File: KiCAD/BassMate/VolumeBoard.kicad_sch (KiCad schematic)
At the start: 15 parts

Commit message: Started docs
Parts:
- added #J?: AudioJack3_Dual_Switch, symbol Connector:AudioJack3_Dual_Switch
- added J?: 1x5, Connector_PinHeader_2.54mm:PinHeader_1x05_P2.54mm_Vertical, symbol Connector_Generic:Conn_01x05
- J?: value To Headphone Socket -> 1x5
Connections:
- new net: #J?.R1, J?.4 (Pin_4)
- new net: #J?.RN1, J?.5 (Pin_5)
- new net: #J?.S1, J?.1 (Pin_1)
- new net: #J?.SN1, J?.2 (Pin_2)
- new net: #J?.T1, #J?.TN1, J?.3 (Pin_3)
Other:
- note added: "Headphone socket on daughter board"
- note added: "Power and I/O"
- note added: "Volume control"
- moved on the sheet: C?, J?, R?, U?A, U?B, U?C, U?D, U?E

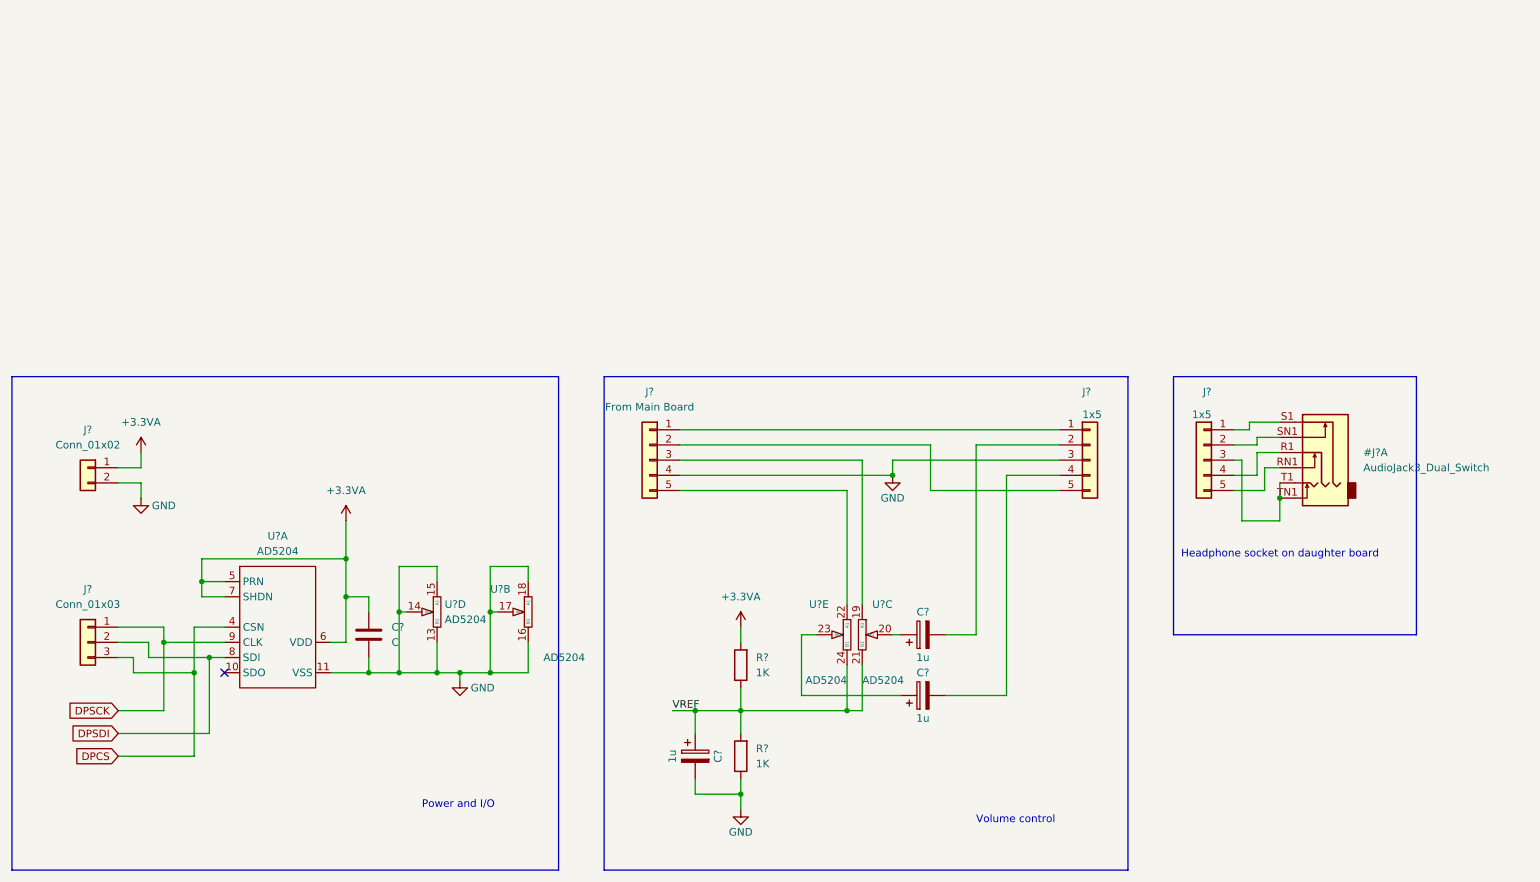
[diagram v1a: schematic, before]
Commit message: Converted most libs to git sbmodules
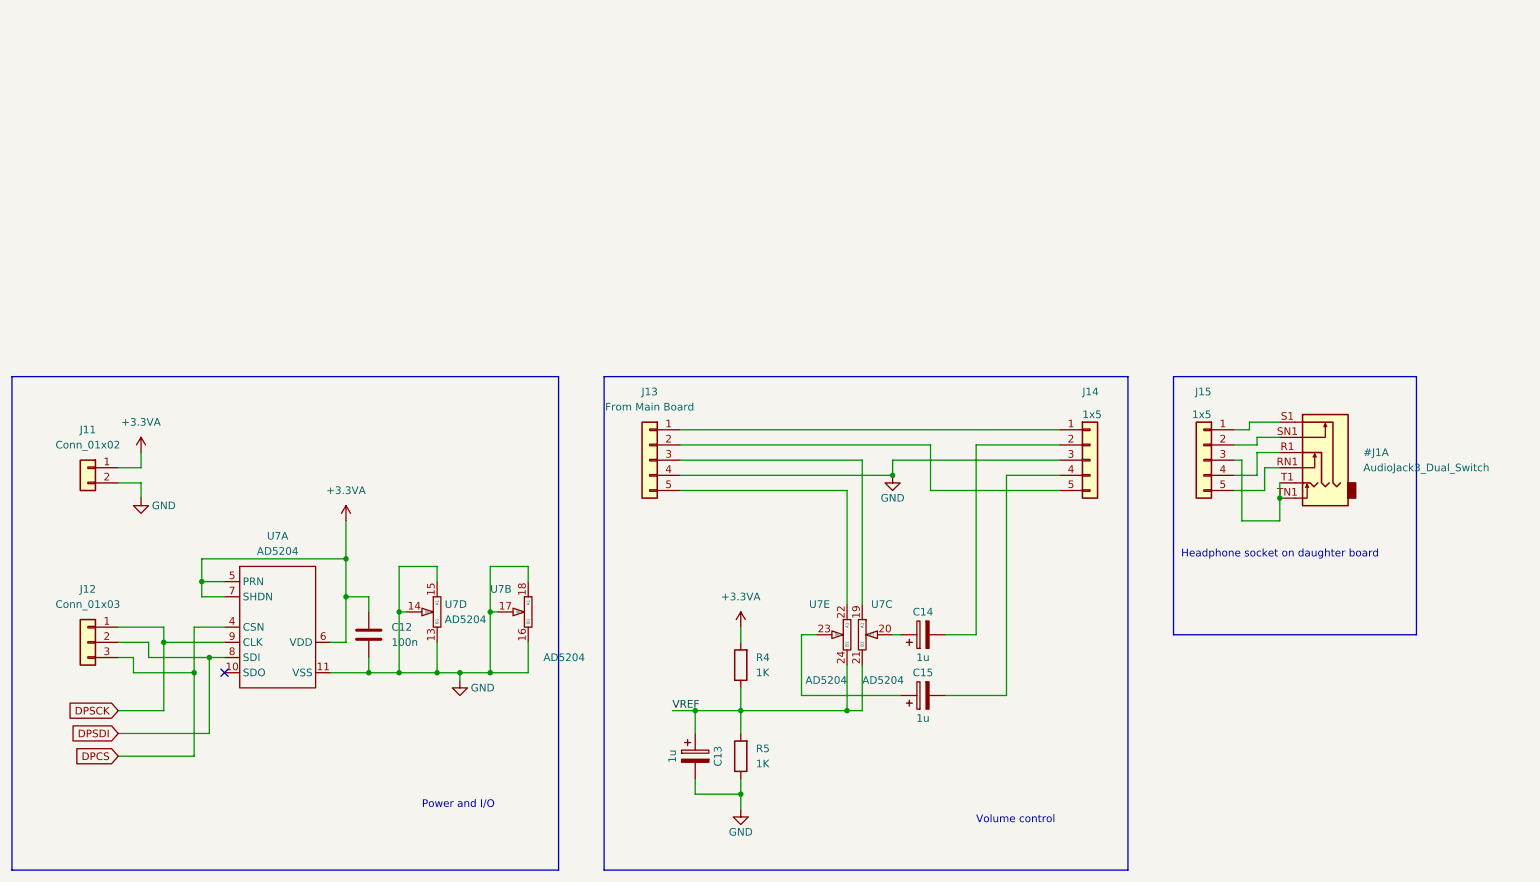
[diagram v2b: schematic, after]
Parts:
- C12: renamed from C?; value C -> 100n
- gave numbers to parts that had none: 12
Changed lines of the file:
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@@
   (symbol (lib_id "Device:C_Polarized") (at 173.99 119.38 90) (unit 1)
     (in_bom yes) (on_board yes)
-    (property "Reference" "C?" (id 0) (at 173.99 115.57 90))
+    (property "Reference" "C14" (id 0) (at 173.99 115.57 90))
     (property "Value" "1u" (id 1) (at 173.99 123.19 90))
     (property "Footprint" "Capacitor_THT:CP_Radial_D10.0mm_P3.50mm" (id 2) (at 177.8 118.4148 0)
@@
   (symbol (lib_id "power:+3.3VA") (at 43.18 88.9 0) (unit 1)
     (in_bom yes) (on_board yes) (fields_autoplaced)
-    (property "Reference" "#PWR?" (id 0) (at 43.18 92.71 0)
+    (property "Reference" "#PWR024" (id 0) (at 43.18 92.71 0)
       (effects (font (size 1.27 1.27)) hide)
     )
@@
   (symbol (lib_id "power:+3.3VA") (at 77.47 100.33 0) (unit 1)
     (in_bom yes) (on_board yes) (fields_autoplaced)
-    (property "Reference" "#PWR?" (id 0) (at 77.47 104.14 0)
+    (property "Reference" "#PWR026" (id 0) (at 77.47 104.14 0)
       (effects (font (size 1.27 1.27)) hide)
     )
@@
   (symbol (lib_id "UKMaker:AD5204") (at 107.95 115.57 0) (unit 2)
     (in_bom yes) (on_board yes)
-    (property "Reference" "U?" (id 0) (at 101.6 111.76 0)
+    (property "Reference" "U7" (id 0) (at 101.6 111.76 0)
       (effects (font (size 1.27 1.27)) (justify left))
     )
@@
   (symbol (lib_id "UKMaker:AD5204") (at 163.83 119.38 0) (mirror y) (unit 3)
     (in_bom yes) (on_board yes)
-    (property "Reference" "U?" (id 0) (at 168.91 114.3 0)
+    (property "Reference" "U7" (id 0) (at 168.91 114.3 0)
       (effects (font (size 1.27 1.27)) (justify left))
     )
@@
   (symbol (lib_id "power:+3.3VA") (at 143.51 118.11 0) (unit 1)
     (in_bom yes) (on_board yes) (fields_autoplaced)
-    (property "Reference" "#PWR?" (id 0) (at 143.51 121.92 0)
+    (property "Reference" "#PWR028" (id 0) (at 143.51 121.92 0)
       (effects (font (size 1.27 1.27)) hide)
     )
@@
   (symbol (lib_id "Connector:AudioJack3_Dual_Switch") (at 238.76 88.9 0) (mirror y) (unit 1)
     (in_bom yes) (on_board yes) (fields_autoplaced)
-    (property "Reference" "#J?" (id 0) (at 247.65 88.8999 0)
+    (property "Reference" "#J1" (id 0) (at 247.65 88.8999 0)
       (effects (font (size 1.27 1.27)) (justify right))
     )
@@
   (symbol (lib_id "Device:C") (at 81.28 119.38 0) (unit 1)
     (in_bom yes) (on_board yes) (fields_autoplaced)
-    (property "Reference" "C?" (id 0) (at 85.09 118.1099 0)
-      (effects (font (size 1.27 1.27)) (justify left))
-    )
-    (property "Value" "C" (id 1) (at 85.09 120.6499 0)
+    (property "Reference" "C12" (id 0) (at 85.09 118.1099 0)
+      (effects (font (size 1.27 1.27)) (justify left))
+    )
+    (property "Value" "100n" (id 1) (at 85.09 120.6499 0)
       (effects (font (size 1.27 1.27)) (justify left))
     )
@@
   (symbol (lib_id "Device:R") (at 143.51 139.7 180) (unit 1)
     (in_bom yes) (on_board yes) (fields_autoplaced)
-    (property "Reference" "R?" (id 0) (at 146.05 138.4299 0)
+    (property "Reference" "R5" (id 0) (at 146.05 138.4299 0)
       (effects (font (size 1.27 1.27)) (justify right))
     )
@@
   (symbol (lib_id "Device:R") (at 143.51 124.46 180) (unit 1)
     (in_bom yes) (on_board yes) (fields_autoplaced)
-    (property "Reference" "R?" (id 0) (at 146.05 123.1899 0)
+    (property "Reference" "R4" (id 0) (at 146.05 123.1899 0)
       (effects (font (size 1.27 1.27)) (justify right))
     )
@@
   (symbol (lib_id "power:GND") (at 96.52 127 0) (unit 1)
     (in_bom yes) (on_board yes)
-    (property "Reference" "#PWR?" (id 0) (at 96.52 133.35 0)
+    (property "Reference" "#PWR027" (id 0) (at 96.52 133.35 0)
       (effects (font (size 1.27 1.27)) hide)
     )
@@
   (symbol (lib_id "power:GND") (at 43.18 96.52 0) (unit 1)
     (in_bom yes) (on_board yes)
-    (property "Reference" "#PWR?" (id 0) (at 43.18 102.87 0)
+    (property "Reference" "#PWR025" (id 0) (at 43.18 102.87 0)
       (effects (font (size 1.27 1.27)) hide)
     )
@@
   (symbol (lib_id "UKMaker:AD5204") (at 92.71 115.57 0) (unit 4)
     (in_bom yes) (on_board yes) (fields_autoplaced)
-    (property "Reference" "U?" (id 0) (at 93.98 114.2999 0)
+    (property "Reference" "U7" (id 0) (at 93.98 114.2999 0)
       (effects (font (size 1.27 1.27)) (justify left))
     )
@@
   (symbol (lib_id "Connector_Generic:Conn_01x05") (at 128.27 90.17 0) (mirror y) (unit 1)
     (in_bom yes) (on_board yes) (fields_autoplaced)
-    (property "Reference" "J?" (id 0) (at 128.27 78.74 0))
+    (property "Reference" "J13" (id 0) (at 128.27 78.74 0))
     (property "Value" "From Main Board" (id 1) (at 128.27 81.28 0))
     (property "Footprint" "Connector_PinHeader_2.54mm:PinHeader_1x05_P2.54mm_Vertical" (id 2) (at 128.27 90.17 0)
@@
   (symbol (lib_id "Connector_Generic:Conn_01x02") (at 34.29 91.44 0) (mirror y) (unit 1)
     (in_bom yes) (on_board yes) (fields_autoplaced)
-    (property "Reference" "J?" (id 0) (at 34.29 85.09 0))
+    (property "Reference" "J11" (id 0) (at 34.29 85.09 0))
     (property "Value" "Conn_01x02" (id 1) (at 34.29 87.63 0))
     (property "Footprint" "" (id 2) (at 34.29 91.44 0)
@@
   (symbol (lib_id "UKMaker:AD5204") (at 161.29 119.38 0) (unit 5)
     (in_bom yes) (on_board yes)
-    (property "Reference" "U?" (id 0) (at 154.94 114.3 0)
+    (property "Reference" "U7" (id 0) (at 154.94 114.3 0)
       (effects (font (size 1.27 1.27)) (justify left))
     )
@@
   (symbol (lib_id "Device:C_Polarized") (at 173.99 129.54 90) (unit 1)
     (in_bom yes) (on_board yes)
-    (property "Reference" "C?" (id 0) (at 173.99 125.73 90))
+    (property "Reference" "C15" (id 0) (at 173.99 125.73 90))
     (property "Value" "1u" (id 1) (at 173.99 133.35 90))
     (property "Footprint" "Capacitor_THT:CP_Radial_D10.0mm_P3.50mm" (id 2) (at 177.8 128.5748 0)
@@
   (symbol (lib_id "power:GND") (at 168.91 92.71 0) (mirror y) (unit 1)
     (in_bom yes) (on_board yes)
-    (property "Reference" "#PWR?" (id 0) (at 168.91 99.06 0)
+    (property "Reference" "#PWR030" (id 0) (at 168.91 99.06 0)
       (effects (font (size 1.27 1.27)) hide)
     )
@@
   (symbol (lib_id "UKMaker:AD5204") (at 66.04 118.11 0) (unit 1)
     (in_bom yes) (on_board yes) (fields_autoplaced)
-    (property "Reference" "U?" (id 0) (at 66.04 102.87 0))
+    (property "Reference" "U7" (id 0) (at 66.04 102.87 0))
     (property "Value" "AD5204" (id 1) (at 66.04 105.41 0))
     (property "Footprint" "" (id 2) (at 69.215 113.03 0)
@@
   (symbol (lib_id "Connector_Generic:Conn_01x05") (at 220.98 90.17 0) (mirror y) (unit 1)
     (in_bom yes) (on_board yes)
-    (property "Reference" "J?" (id 0) (at 222.25 78.74 0)
+    (property "Reference" "J15" (id 0) (at 222.25 78.74 0)
       (effects (font (size 1.27 1.27)) (justify left))
     )
@@
   (symbol (lib_id "power:GND") (at 143.51 148.59 0) (mirror y) (unit 1)
     (in_bom yes) (on_board yes)
-    (property "Reference" "#PWR?" (id 0) (at 143.51 154.94 0)
+    (property "Reference" "#PWR029" (id 0) (at 143.51 154.94 0)
       (effects (font (size 1.27 1.27)) hide)
     )
@@
   (symbol (lib_id "Device:C_Polarized") (at 135.89 139.7 0) (unit 1)
     (in_bom yes) (on_board yes)
-    (property "Reference" "C?" (id 0) (at 139.7 139.7 90))
+    (property "Reference" "C13" (id 0) (at 139.7 139.7 90))
     (property "Value" "1u" (id 1) (at 132.08 139.7 90))
     (property "Footprint" "Capacitor_THT:CP_Radial_D10.0mm_P3.50mm" (id 2) (at 136.8552 143.51 0)
@@
   (symbol (lib_id "Connector_Generic:Conn_01x05") (at 201.93 90.17 0) (unit 1)
     (in_bom yes) (on_board yes)
-    (property "Reference" "J?" (id 0) (at 200.66 78.74 0)
+    (property "Reference" "J14" (id 0) (at 200.66 78.74 0)
       (effects (font (size 1.27 1.27)) (justify left))
     )
@@
   (symbol (lib_id "Connector_Generic:Conn_01x03") (at 34.29 120.65 0) (mirror y) (unit 1)
     (in_bom yes) (on_board yes) (fields_autoplaced)
-    (property "Reference" "J?" (id 0) (at 34.29 111.76 0))
+    (property "Reference" "J12" (id 0) (at 34.29 111.76 0))
     (property "Value" "Conn_01x03" (id 1) (at 34.29 114.3 0))
     (property "Footprint" "" (id 2) (at 34.29 120.65 0)
